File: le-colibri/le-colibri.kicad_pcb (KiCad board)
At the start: 2 copper layers, 225.8 x 89.3 mm, 63 parts, among them SW1 CPG151101S11, SW10 CPG151101S11, SW11 CPG151101S11, SW12 CPG151101S11, SW13 CPG151101S11, SW14 CPG151101S11, SW15 CPG151101S11, SW16 CPG151101S11, SW17 CPG151101S11, SW18 CPG151101S11, SW19 CPG151101S11, SW2 CPG151101S11, SW20 CPG151101S11, SW21 CPG151101S11, SW22 CPG151101S11, SW23 CPG151101S11, SW24 CPG151101S11, SW25 CPG151101S11, SW26 CPG151101S11, SW27 CPG151101S11, SW28 CPG151101S11, SW29 CPG151101S11, SW3 CPG151101S11, SW30 CPG151101S11, SW4 CPG151101S11, SW5 CPG151101S11, SW6 CPG151101S11, SW7 CPG151101S11, SW8 CPG151101S11, SW9 CPG151101S11, U1 Seeeduino Xiao rp2040

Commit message: "first" "release"
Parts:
- added G***: LOGO, LOGO, F.Cu at (151.0, 106.1)
- added G***: LOGO, LOGO, B.Cu at (151.0, 106.1)
- U1: moved to B.Cu
- moved U1 19.9 mm to (150.9, 52.6), turned to 180 degrees
- moved D12 9.73 mm to (85.2, 83.8)
- moved D15 9.73 mm to (110.7, 110.9)
- moved D5 9.73 mm to (125.9, 64.8)
- moved D6 9.73 mm to (48.0, 74.4)
- moved D9 9.73 mm to (105.8, 71.9)
- moved SW1 9.73 mm to (49.7, 60.6)
- moved SW11 9.73 mm to (65.1, 91.3)
- moved SW12 9.73 mm to (84.6, 88.9)
- moved SW14 9.73 mm to (79.3, 112.2)
- moved SW8 9.73 mm to (86.9, 69.9)
- moved SW9 9.73 mm to (105.2, 77.0)
- moved D3 9.73 mm to (89.8, 46.0)
- moved SW3 9.73 mm to (89.2, 51.0)
- moved SW4 9.73 mm to (107.6, 58.1)
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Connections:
- U1 pad 1: unconnected-(U1-P26-Pad1) -> R4
- U1 pad 11: unconnected-(U1-P3-Pad11) -> R1
- U1 pad 12: unconnected-(U1-P4-Pad12) -> R2
- U1 pad 13: unconnected-(U1-P2-Pad13) -> R3
- U1 pad 14: unconnected-(U1-P1-Pad14) -> C5
- U1 pad 2: unconnected-(U1-P27-Pad2) -> R5
- U1 pad 3: unconnected-(U1-P28-Pad3) -> R6
- U1 pad 4: unconnected-(U1-P29-Pad4) -> C1
- U1 pad 5: unconnected-(U1-P6-Pad5) -> C2
- U1 pad 6: unconnected-(U1-P7-Pad6) -> C3
- U1 pad 7: unconnected-(U1-P0-Pad7) -> C4
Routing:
- net C1: track 0.00 -> 397.3 mm, vias 0 -> 1
- net C2: track 0.00 -> 270.0 mm, vias 0 -> 1
- net C3: track 0.00 -> 221.4 mm, vias 0 -> 1
- net C5: track 0.00 -> 186.0 mm
- net R6: track 0.00 -> 175.7 mm
- net C4: track 0.00 -> 174.0 mm, vias 0 -> 1
- net R3: track 0.00 -> 173.4 mm
- net R5: track 0.00 -> 132.5 mm
- net R2: track 0.00 -> 129.9 mm
- net R4: track 0.00 -> 120.5 mm
- net R1: track 0.00 -> 111.6 mm
- net Net-(D16-K): track 0.00 -> 11.3 mm
- net Net-(D17-K): track 0.00 -> 11.1 mm
- net Net-(D14-K): track 0.00 -> 10.7 mm
- net Net-(D18-K): track 0.00 -> 10.2 mm
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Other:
- board size 225.8 x 89.3 mm -> 227.4 x 84.9 mm
- board text added: "Le Colibri"
- board text added: "© 2024 Travis Mick github.com/eggsworks"

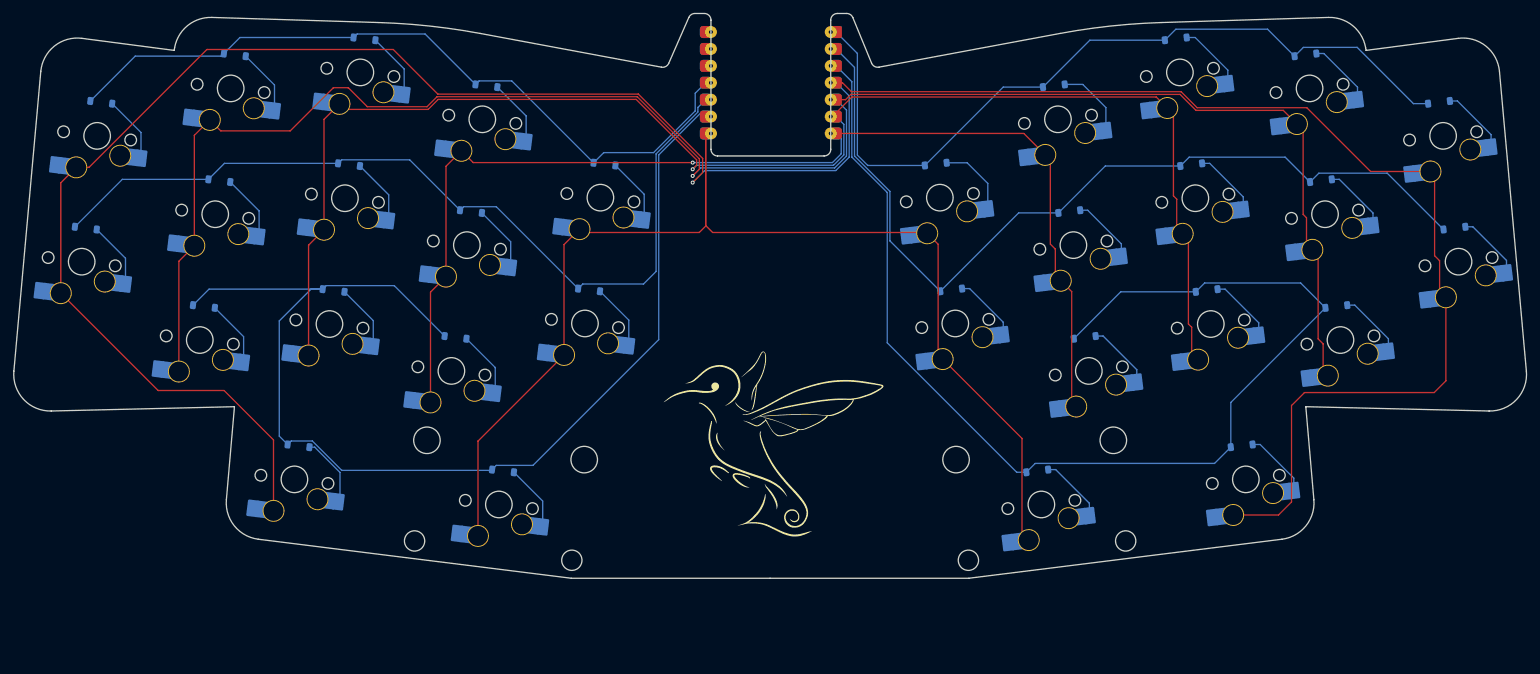
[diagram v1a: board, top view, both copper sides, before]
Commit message: added new options for thumbs and pinkie
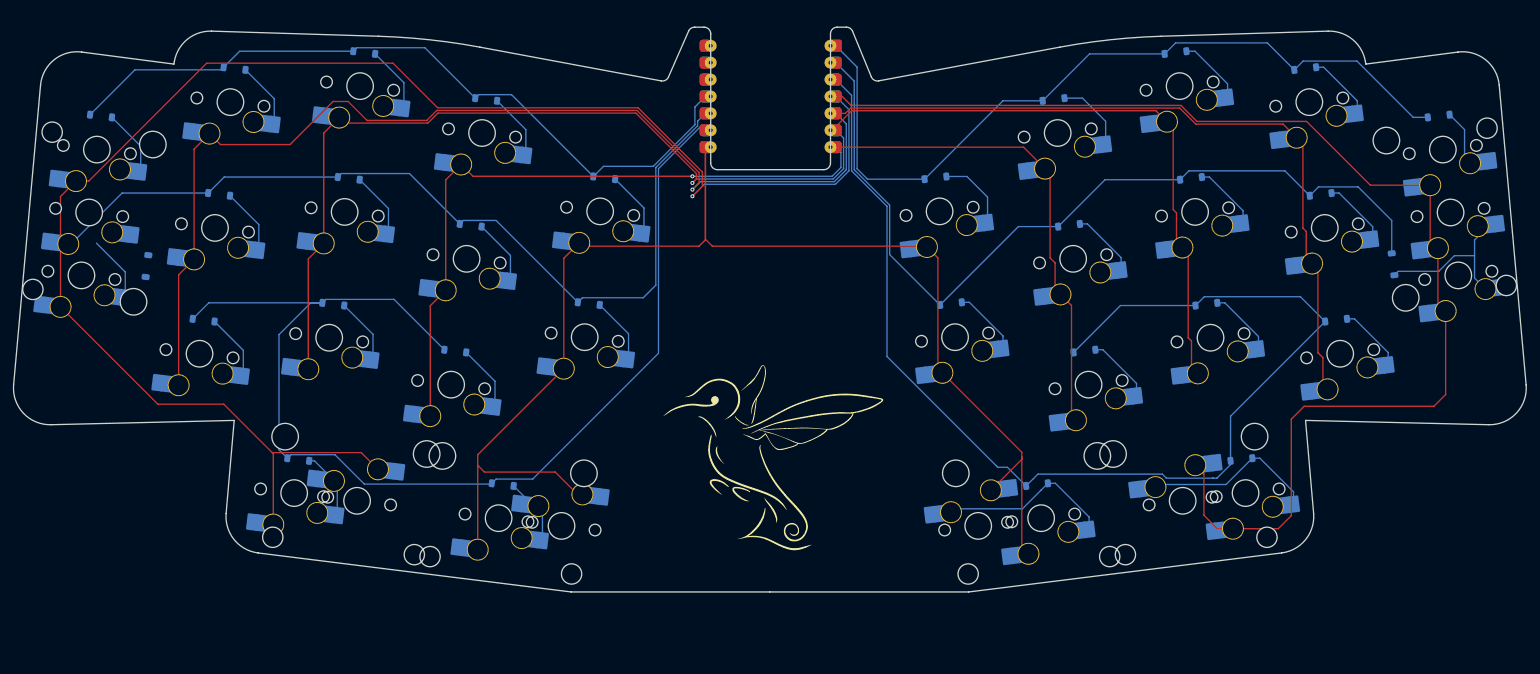
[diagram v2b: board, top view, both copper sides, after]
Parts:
- added REF**: STAB_MX_2u, PCM_marbastlib-mx:STAB_MX_2u, F.Cu at (88.7, 115.4)
- added REF**: STAB_MX_2u, PCM_marbastlib-mx:STAB_MX_2u, F.Cu at (212.8, 115.4)
- added REF**: STAB_MX_2u, PCM_marbastlib-mx:STAB_MX_2u, F.Cu at (253.1, 72.1)
- added REF**: STAB_MX_2u, PCM_marbastlib-mx:STAB_MX_2u, F.Cu at (48.4, 72.7)
- added SW31: CPG151101S11, Library:SW_MX_HS_CPG151101S11_1u, B.Cu at (88.7, 115.4)
- added SW32: CPG151101S11, Library:SW_MX_HS_CPG151101S11_1u, B.Cu at (119.5, 119.2)
- added SW33: CPG151101S11, Library:SW_MX_HS_CPG151101S11_1u, B.Cu at (182.1, 119.2)
- added SW34: CPG151101S11, Library:SW_MX_HS_CPG151101S11_1u, B.Cu at (212.8, 115.4)
- added SW35: CPG151101S11, Library:SW_MX_HS_CPG151101S11_1u, B.Cu at (48.5, 72.1)
- added SW36: CPG151101S11, Library:SW_MX_HS_CPG151101S11_1u, B.Cu at (253.1, 72.1)
- moved D6 10.8 mm to (57.2, 80.1), turned to 83 degrees
- moved D25 10.7 mm to (244.4, 79.9), turned to 97 degrees
- moved D10 2.06 mm to (123.6, 85.8)
- moved REF** 2.06 mm to (191.5, 118.0)
- moved SW29 2.06 mm to (191.5, 118.0)
- moved SW24 2.06 mm to (234.2, 74.4)
- moved D20 2.06 mm to (251.3, 57.6)
- moved SW30 2.06 mm to (222.3, 114.3)
- moved D22 2.06 mm to (195.7, 74.0)
- moved U1 2.06 mm to (150.9, 54.7)
- moved D28 2.06 mm to (235.9, 88.3)
- moved SW16 2.06 mm to (176.3, 71.9)
- moved SW2 2.06 mm to (69.7, 55.5)
- moved SW5 2.06 mm to (125.3, 71.9)
- moved D17 2.06 mm to (193.4, 55.1)
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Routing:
- net C1: track 397.3 -> 429.7 mm
- net C5: track 186.0 -> 210.4 mm
- net Net-(D30-K): track 10.1 -> 29.8 mm
- net Net-(D29-K): track 10.1 -> 28.4 mm
- net Net-(D25-K): track 10.1 -> 24.6 mm
- net R5: track 132.5 -> 128.3 mm
- net Net-(D20-K): track 10.1 -> 8.57 mm
- net R6: track 175.7 -> 176.6 mm

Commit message: Fixups and switchplates for alt layout
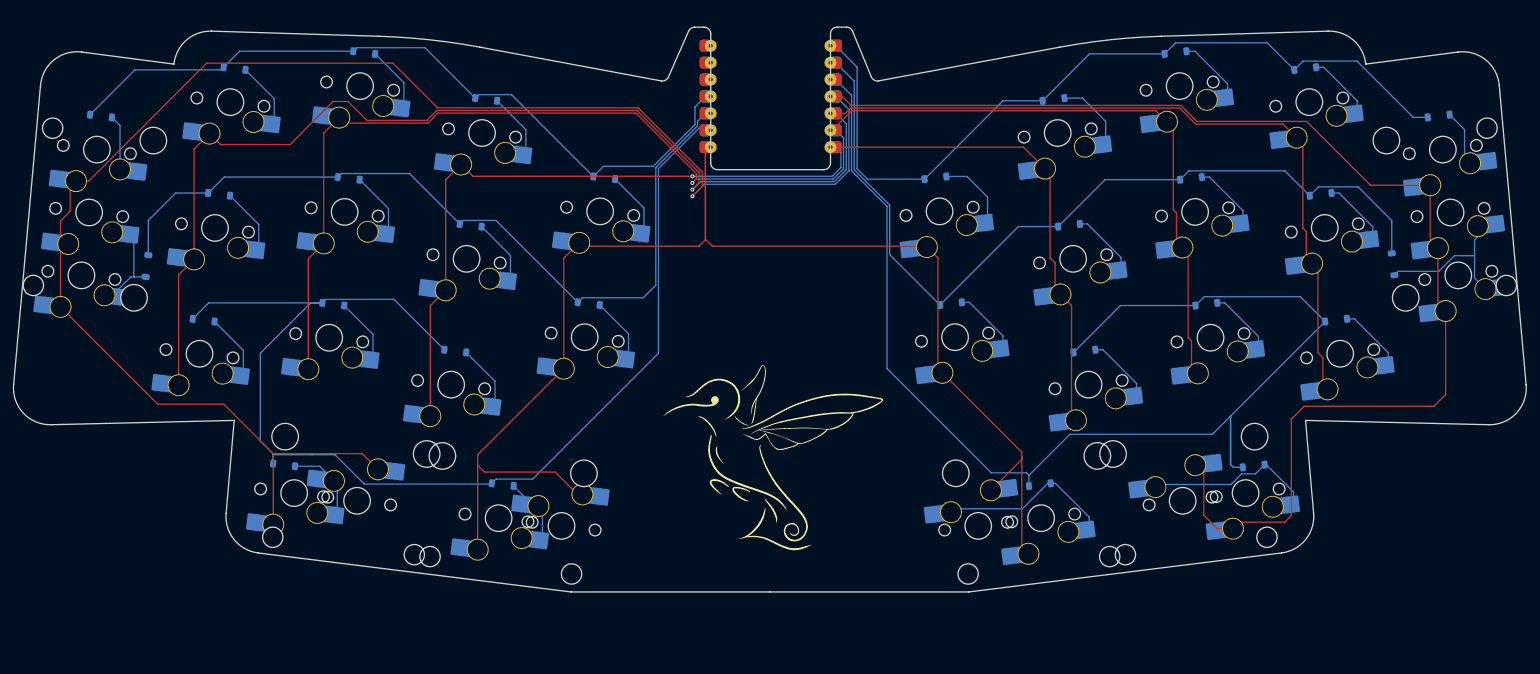
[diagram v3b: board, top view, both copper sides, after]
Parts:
- moved D14 2.28 mm to (77.8, 110.0)
- moved D30 2.09 mm to (223.5, 110.2)
- moved REF** 0.60 mm to (48.5, 72.1)
- moved D29 0.43 mm to (191.3, 113.0)
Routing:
- net R6: track 176.6 -> 189.7 mm
- net R2: track 129.9 -> 122.8 mm
- net C3: track 221.4 -> 214.5 mm
- net C1: track 429.7 -> 424.7 mm
- net C2: track 270.0 -> 265.2 mm
- net Net-(D6-K): track 10.0 -> 14.6 mm
- net C5: track 210.4 -> 206.5 mm
- net C4: track 174.0 -> 170.8 mm
- net R3: track 173.4 -> 176.5 mm
- net Net-(D14-K): track 10.5 -> 12.1 mm
- net Net-(D20-K): track 8.57 -> 7.40 mm
- net Net-(D1-K): track 10.0 -> 11.1 mm
- net Net-(D30-K): track 29.8 -> 29.0 mm
